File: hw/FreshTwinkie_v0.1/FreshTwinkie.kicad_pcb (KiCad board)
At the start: 2 copper layers, 35.4 x 35.3 mm, 54 parts, among them J1 USB_C_Receptacle, J2 USB_B_Micro, P1 USB_C_Plug, Q1 BSD84, Q2 BSD84, Q3 BSD84, Q4 BSD84, SW1 SW_Push, U1 AD8606, U2 STM32F072CBUx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

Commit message: routingSW&Boot
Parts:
- C4, FB1: moved to F.Cu
- moved R2 59.2 mm to (130.5, 66.6), turned to 180 degrees
- moved C4 53.8 mm to (134.5, 64.9), turned to 180 degrees
- moved FB1 52.5 mm to (137.6, 64.9), turned to 180 degrees
- moved R18 33.8 mm to (132.8, 68.0), turned to 90 degrees
- moved R19 31.9 mm to (134.3, 68.0), turned to 90 degrees
- moved R20 30.3 mm to (135.9, 68.0), turned to 90 degrees
- moved R16 28.8 mm to (137.4, 68.0), turned to 90 degrees
- moved R17 27.7 mm to (139.0, 68.0), turned to 90 degrees
- moved R22 27.3 mm to (149.2, 70.5)
- moved R24 26.6 mm to (149.4, 78.3)
- moved Q4 26.5 mm to (147.2, 75.9)
- moved R14 23.8 mm to (148.1, 73.7)
- moved R15 23.8 mm to (148.1, 72.1)
- moved U3 23.7 mm to (151.4, 79.3), turned to 0 degrees
- moved SW1 23.3 mm to (144.9, 83.3)
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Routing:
- net GND: track 65.6 -> 104.5 mm, vias 1 -> 3
- net +3V3: track 24.9 -> 45.9 mm
- net Net-(D2-Pad1): track 0.00 -> 15.0 mm, vias 0 -> 1
- net /BOOT: track 0.00 -> 12.9 mm
- net /USB_B_ID: track 0.00 -> 12.1 mm
- net Net-(C8-Pad1): track 0.00 -> 10.3 mm, vias 0 -> 1
- net /SCL: track 0.00 -> 7.86 mm
- net /SDA: track 0.00 -> 7.09 mm
- net /CC2_RA: track 0.00 -> 6.69 mm, vias 0 -> 1
- net Net-(R24-Pad1): track 0.00 -> 6.55 mm, vias 0 -> 1
- net /CC2_RD: track 0.00 -> 6.19 mm, vias 0 -> 1
- net /CC2_RPUSB: track 0.00 -> 5.43 mm, vias 0 -> 1
- net Net-(C4-Pad1): track 0.00 -> 4.89 mm
- net /CC2_RP3A0: track 0.00 -> 3.44 mm, vias 0 -> 1
- net /CC2_RP1A5: track 0.00 -> 3.16 mm, vias 0 -> 1
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
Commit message: routingC6-9
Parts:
- R8: moved to F.Cu
- moved TP1 49.3 mm to (151.9, 65.2)
- moved NT1 25.3 mm to (135.1, 69.8), turned to 0 degrees
- moved C6 21.3 mm to (142.3, 67.6)
- moved C9 21.3 mm to (145.5, 67.7)
- moved C7 21.3 mm to (144.0, 67.6)
- moved R1 13.5 mm to (129.0, 74.9)
- moved R12 13.5 mm to (129.0, 76.4)
- moved R8 11.0 mm to (127.0, 79.1), turned to 180 degrees
- moved C5 4.14 mm to (106.2, 86.0)
- moved Q2 4.14 mm to (102.1, 90.6)
- moved Q3 4.14 mm to (102.1, 94.0)
- moved R13 4.14 mm to (104.5, 95.1)
- moved R21 4.14 mm to (113.0, 83.1)
- moved Q1 4.14 mm to (102.1, 87.4)
- moved U1 4.14 mm to (105.4, 84.4)
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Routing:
- net /NRST: track 0.00 -> 16.6 mm, vias 0 -> 2
- net +3V3: track 45.9 -> 60.0 mm
- net /TX_CLKOUT: track 0.00 -> 9.54 mm, vias 0 -> 2
- net GND: track 104.5 -> 110.0 mm
- net /CC2_RD: track 6.19 -> 7.76 mm
- net /TX_CLKIN: track 0.00 -> 0.93 mm

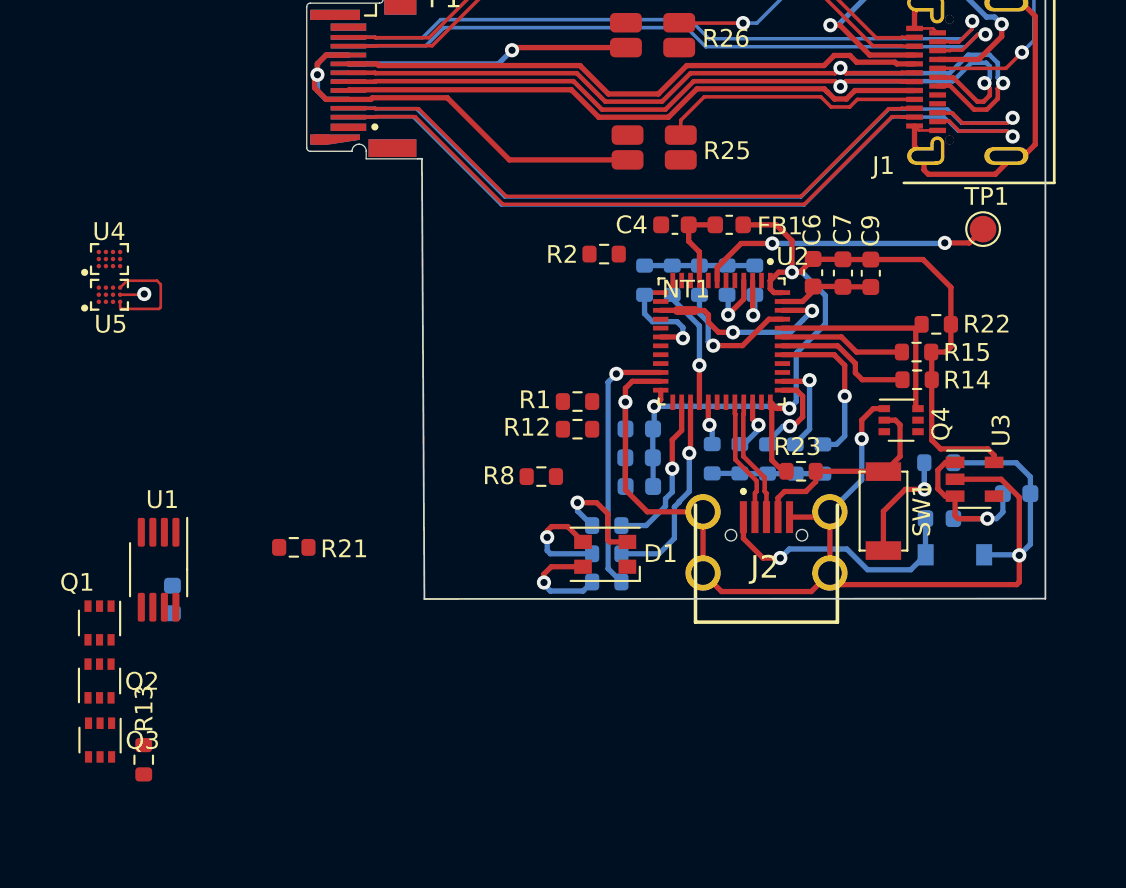
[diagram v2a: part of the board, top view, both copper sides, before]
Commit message: routingC4-5,FB1
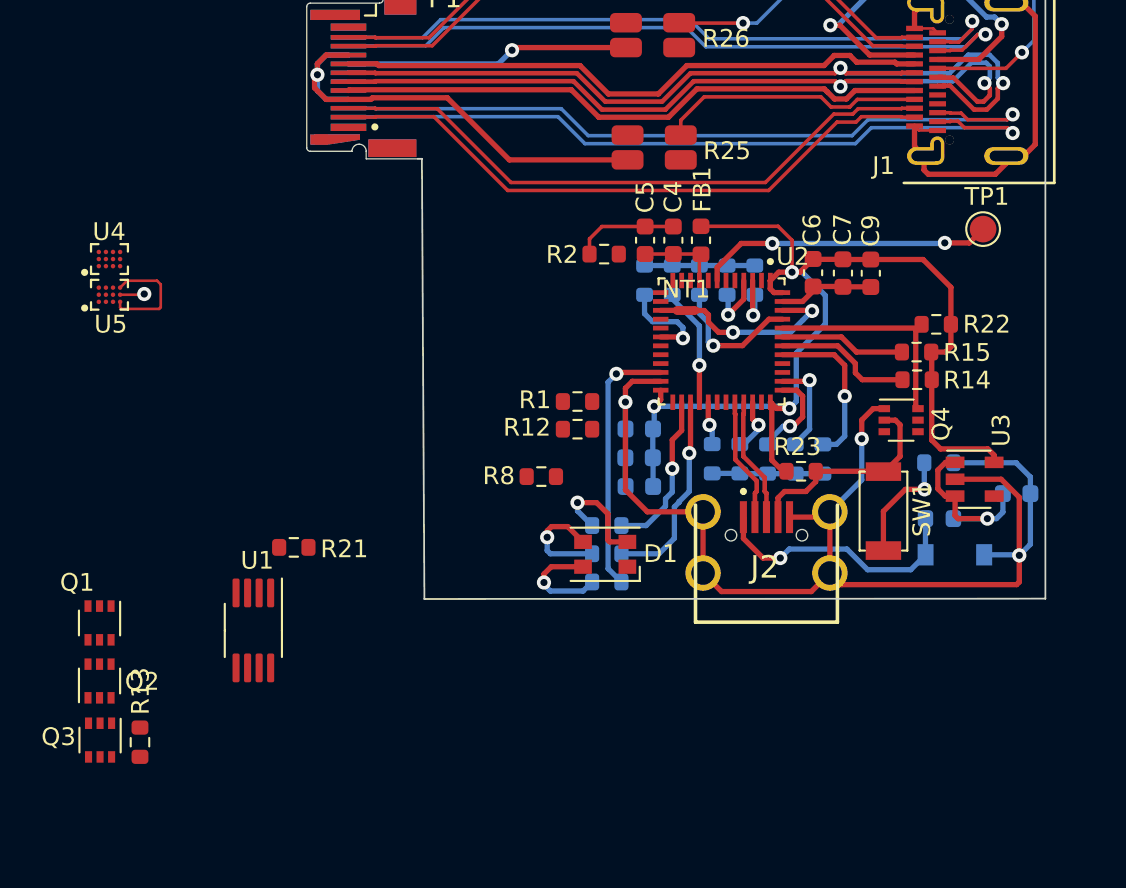
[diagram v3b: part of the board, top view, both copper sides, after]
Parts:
- C5: moved to F.Cu
- moved C5 33.5 mm to (132.8, 65.8)
- moved U1 6.34 mm to (110.7, 87.8)
- moved FB1 1.81 mm to (136.0, 65.8), turned to 270 degrees
- moved R13 1.01 mm to (104.3, 94.1)
- moved C4 0.87 mm to (134.4, 65.8), turned to 90 degrees
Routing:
- net GND: track 110.0 -> 115.8 mm
- net /RX1-: track 46.6 -> 43.1 mm
- net /RX1+: track 46.6 -> 43.1 mm
- net +3V3: track 60.0 -> 62.4 mm
- net /TX1-: track 36.0 -> 35.4 mm
- net /TX1+: track 36.0 -> 35.4 mm

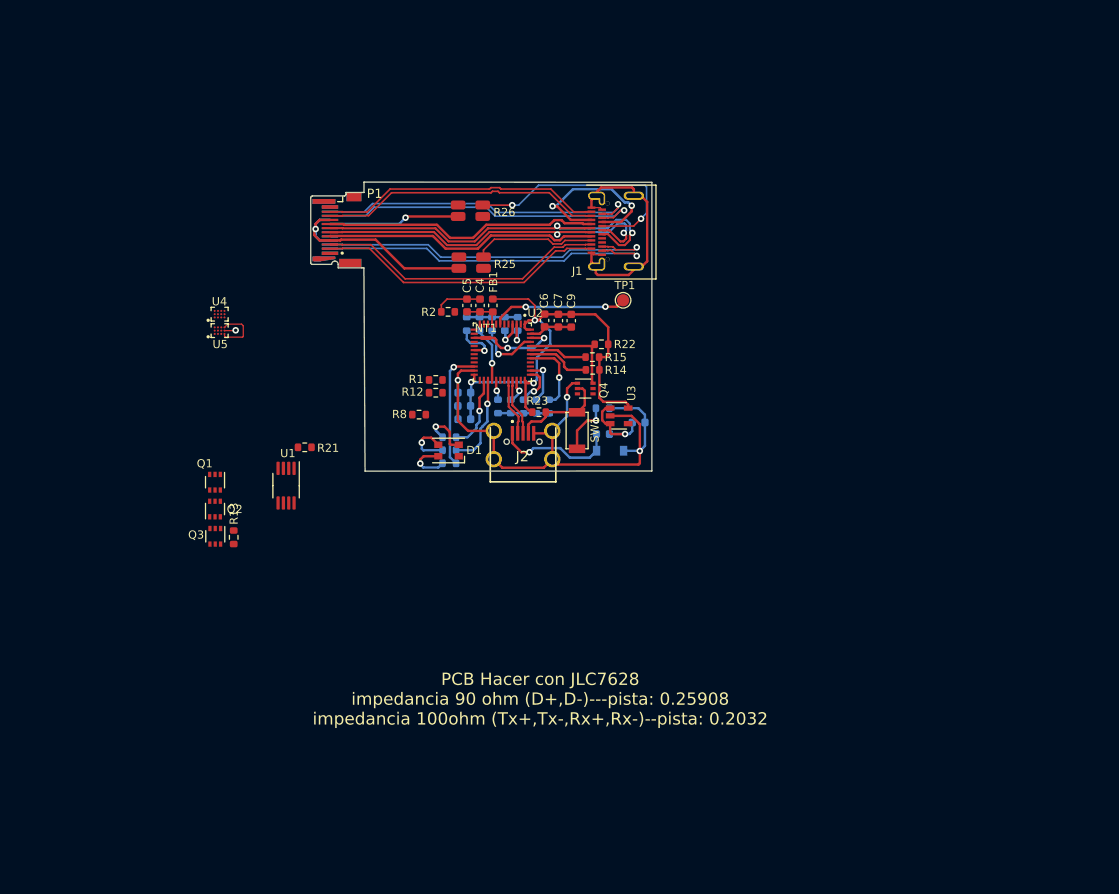
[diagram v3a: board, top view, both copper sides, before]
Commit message: changeINA231forINA226
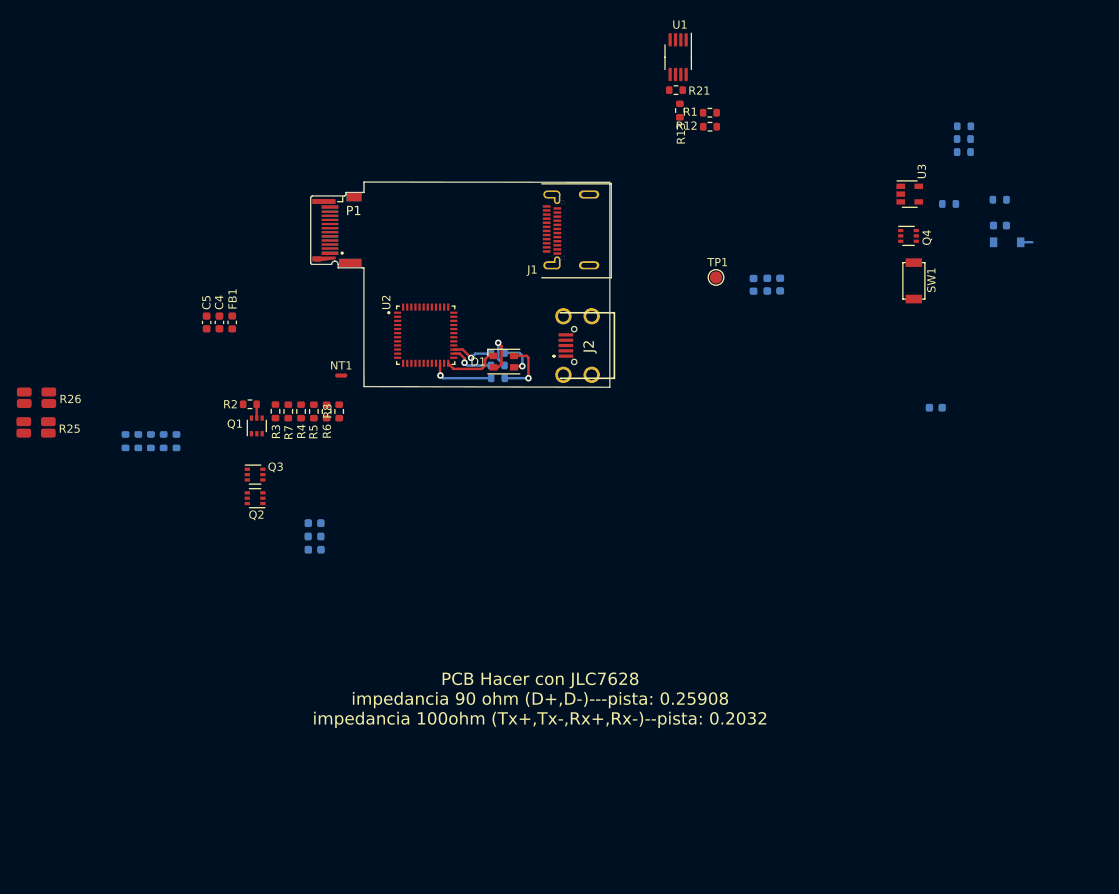
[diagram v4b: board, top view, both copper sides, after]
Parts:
- removed U4, U5: INA231, BGA12N40P3X4_119X159X62N:BGA12N40P3X4_119X159X62N
- C6, C7, C9, R14, R15, R22, R23: moved to B.Cu
- R3, R4, R5, R6, R7: moved to F.Cu
- moved R13 75.3 mm to (158.8, 42.0)
- moved U1 70.9 mm to (158.6, 35.5)
- moved R21 62.9 mm to (158.3, 39.5)
- moved R26 57.7 mm to (80.3, 77.0)
- moved R25 56.8 mm to (80.2, 80.7)
- moved R23 56.1 mm to (191.6, 53.4)
- moved D2 54.7 mm to (198.7, 58.1)
- moved FB2 54.7 mm to (197.8, 56.0)
- moved R24 54.7 mm to (197.8, 52.9)
- moved R14 54.2 mm to (193.5, 43.9)
- moved R15 52.6 mm to (193.4, 45.5)
- moved R22 50.1 mm to (193.4, 47.1)
- moved R1 46.7 mm to (162.4, 42.3)
- moved R12 46.6 mm to (162.5, 44.0)
- moved SW1 45.0 mm to (186.0, 65.0)
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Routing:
- net GND: track 115.8 -> 1.44 mm, vias 3 -> 0
- net +3V3: track 62.4 -> 6.96 mm, vias 3 -> 0
- net /USBC_D-: track 49.6 -> 0.00 mm, vias 2 -> 0
- net /USBC_D+: track 48.1 -> 0.00 mm, vias 2 -> 0
- net /RX1-: track 43.1 -> 0.00 mm, vias 1 -> 0
- net /RX1+: track 43.1 -> 0.00 mm, vias 1 -> 0
- net /TX2-: track 40.1 -> 0.00 mm, vias 1 -> 0
- net /TX2+: track 39.4 -> 0.00 mm, vias 1 -> 0
- net Net-(J1-PadA4): track 36.6 -> 0.00 mm, vias 2 -> 0
- net /TX1+: track 35.4 -> 0.00 mm
- net /TX1-: track 35.4 -> 0.00 mm
- net /RX2-: track 34.4 -> 0.00 mm
- net /RX2+: track 34.4 -> 0.00 mm
- net /USB_C_SBU1: track 33.7 -> 0.00 mm
- net /USBC_CC1: track 33.7 -> 0.00 mm
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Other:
- board size 35.4 x 35.3 mm -> 30.3 x 25 mm

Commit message: changesizeofPCB&routing
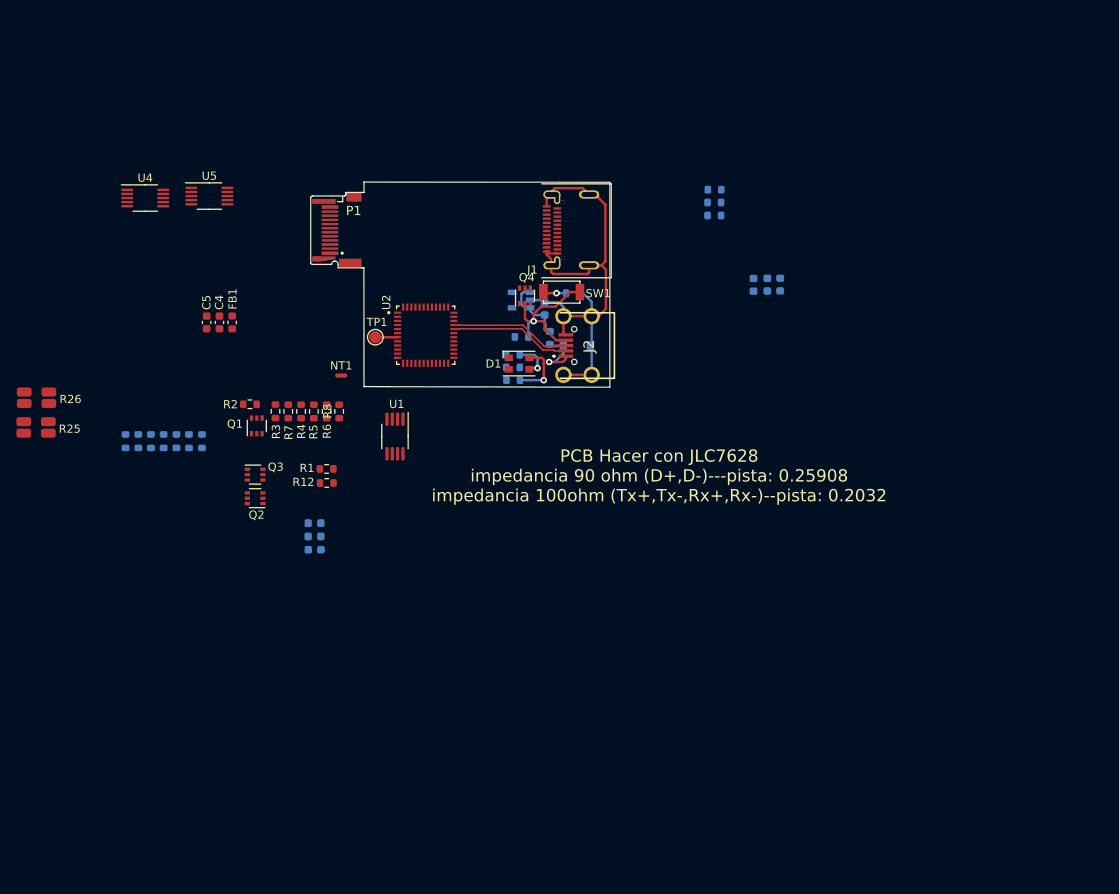
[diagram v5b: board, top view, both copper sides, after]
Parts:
- added U4: INA226, Package_SO:VSSOP-10_3x3mm_P0.5mm, F.Cu at (93.5, 52.7)
- added U5: INA226, Package_SO:VSSOP-10_3x3mm_P0.5mm, F.Cu at (101.4, 52.4)
- Q1, Q2, Q3, Q4: value BSD84 -> BSD840NH6327XTSA1
- R13, R21, U3: moved to B.Cu
- U1: value AD8606 -> AD8606ARMZ-REEL
- moved R13 72.2 mm to (98.9, 82.3), turned to 90 degrees
- moved R21 72.0 mm to (100.5, 82.3), turned to 270 degrees
- moved R12 63.9 mm to (115.7, 87.5)
- moved R1 63.9 mm to (115.7, 85.7)
- moved U1 57.8 mm to (124.0, 81.8)
- moved FB2 56.6 mm to (142.9, 69.8), turned to 270 degrees
- moved R23 54.6 mm to (139.5, 69.6)
- moved D2 54.0 mm to (146.2, 70.7)
- moved R24 53.3 mm to (145.7, 64.3)
- moved C8 49.2 mm to (142.3, 66.2), turned to 90 degrees
- moved U3 49.2 mm to (139.4, 65.1), turned to 180 degrees
- moved Q4 47.4 mm to (139.9, 64.6), turned to 90 degrees
- moved SW1 43.9 mm to (142.1, 62.8), turned to 0 degrees
- moved TP1 42.2 mm to (121.6, 69.7)
- moved R14 31.4 mm to (163.0, 51.7)
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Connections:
- U1 pad 4: GND -> (no net)
- U1 pad 8: +3V3 -> (no net)
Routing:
- net GND: track 1.44 -> 63.2 mm
- net /USB_B_ID: track 0.00 -> 18.4 mm, vias 0 -> 1
- net /USB_B_D-: track 0.00 -> 14.8 mm
- net /USB_B_D+: track 0.00 -> 14.8 mm
- net Net-(C8-Pad1): track 0.00 -> 8.51 mm
- net /LED_G_L: track 7.84 -> 0.00 mm, vias 1 -> 0
- net Net-(D2-Pad1): track 0.00 -> 7.35 mm, vias 0 -> 1
- net +3V3: track 6.96 -> 0.00 mm
- net Net-(D1-Pad2): track 6.96 -> 0.00 mm, vias 1 -> 0
- net /LED_R_L: track 5.44 -> 0.00 mm, vias 1 -> 0
- net /LED_B_L: track 5.21 -> 0.00 mm, vias 1 -> 0
- net Net-(R24-Pad1): track 0.00 -> 2.83 mm, vias 0 -> 1
- net /NRST: track 0.00 -> 2.72 mm
- net /CC1_EN: track 1.70 -> 0.00 mm

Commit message: newroutingUSBC
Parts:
- C4, C5, FB1, Q1, R5, R6, U1: moved to B.Cu
- C6, C7, C9, R13, R16, R17, R18, R19, R20, R21: moved to F.Cu
- moved R14 69.2 mm to (144.4, 118.3)
- moved R15 69.2 mm to (144.4, 119.8)
- moved R22 69.2 mm to (144.4, 121.4)
- moved C4 55.7 mm to (138.6, 110.4), turned to 270 degrees
- moved FB1 55.7 mm to (140.2, 110.4), turned to 90 degrees
- moved C5 55.7 mm to (137.0, 110.4), turned to 270 degrees
- moved TP1 54.3 mm to (139.3, 121.0)
- moved R20 51.6 mm to (142.0, 101.8)
- moved R16 48.9 mm to (137.8, 107.3), turned to 180 degrees
- moved R17 46.8 mm to (137.8, 105.8), turned to 180 degrees
- moved C9 46.7 mm to (151.9, 105.8), turned to 270 degrees
- moved C7 46.7 mm to (150.3, 105.8), turned to 270 degrees
- moved C6 46.7 mm to (148.6, 105.8), turned to 270 degrees
- moved R5 46.5 mm to (150.1, 108.1), turned to 0 degrees
- moved R6 46.4 mm to (150.3, 109.7), turned to 0 degrees
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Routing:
- net /USBC_D+: track 0.00 -> 40.0 mm, vias 0 -> 2
- net /USBC_D-: track 0.00 -> 37.3 mm, vias 0 -> 2
- net /CC1: track 0.00 -> 18.8 mm, vias 0 -> 1
- net +3V3: track 0.00 -> 18.6 mm, vias 0 -> 1
- net /BOOT: track 0.00 -> 14.6 mm, vias 0 -> 2
- net Net-(P1-PadA4): track 0.00 -> 11.1 mm, vias 0 -> 1
- net /LED_G_L: track 0.00 -> 10.2 mm, vias 0 -> 1
- net Net-(D1-Pad2): track 0.00 -> 8.10 mm, vias 0 -> 1
- net GND: track 63.2 -> 71.2 mm
- net /LED_R_L: track 0.00 -> 7.44 mm, vias 0 -> 1
- net /LED_B_L: track 0.00 -> 6.88 mm, vias 0 -> 1
- net Net-(C4-Pad1): track 0.00 -> 5.61 mm, vias 0 -> 1
- net /CC1_RPUSB: track 0.00 -> 4.94 mm, vias 0 -> 1
- net /CC1_RP3A0: track 0.00 -> 3.25 mm
- net /CC2: track 0.00 -> 3.12 mm
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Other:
- board size 30.3 x 25 mm -> 30.2 x 25 mm
